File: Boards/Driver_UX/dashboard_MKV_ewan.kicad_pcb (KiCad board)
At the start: 4 copper layers, 57.2 x 41.7 mm, 63 parts, among them J1 MM_F_VT_10, J2 MM_F_VT_20, J3 MM_F_VT_04, J4 CONN_02X03, J5 CONN_02X03, Q1 SSM3K333R, U1 ATMEGA16M1, U101 TPS560430YF, U3 ATmega328P-AU, U4 CAN_Transceiver, Y1 Crystal_SMD, Y2 Crystal_SMD

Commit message: start of new layout
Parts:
- moved D101 99.3 mm to (77.9, 88.1)
- moved J3 99.1 mm to (105.4, 89.4)
- moved J1 99.1 mm to (118.0, 92.1)
- moved J2 99.1 mm to (90.1, 84.9)
- moved C102 98.9 mm to (76.6, 82.3)
- moved C103 98.9 mm to (76.5, 75.9)
- moved D102 98.9 mm to (75.9, 93.4)
- moved D103 98.9 mm to (87.2, 76.9)
- moved L101 98.9 mm to (80.2, 76.4)
- moved R104 98.9 mm to (84.1, 78.7)
- moved R105 98.9 mm to (87.2, 80.7)
- moved C101 98.9 mm to (76.4, 84.1)
- moved COUT101 98.9 mm to (77.8, 71.9)
- moved COUT102 98.9 mm to (84.1, 73.0)
- moved COUT103 98.9 mm to (80.1, 71.9)
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- renumbered PD1 to D3, PD2 to D4, PB5 to D5, PB6 to D6, PC7 to D8
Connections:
- D101 pad 1: /12V -> Net-(C101-Pad1)
- J2 pad 2: +12V -> /12V
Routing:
- net Net-(C13-Pad1): track 13.9 -> 2.25 mm, vias 2 -> 0
- net GND: track 104.2 -> 112.8 mm
- net Net-(C101-Pad1): track 16.9 -> 24.1 mm
- net /SCK: track 21.8 -> 16.7 mm, vias 3 -> 1
- net /12V: track 3.63 -> 0.00 mm
- net /STR_POT_SENSE: track 43.0 -> 39.7 mm, vias 4 -> 2
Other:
- board text removed: "Emily Wan DUX Rev 1.2 | 12/14/19 OEM-MKV"

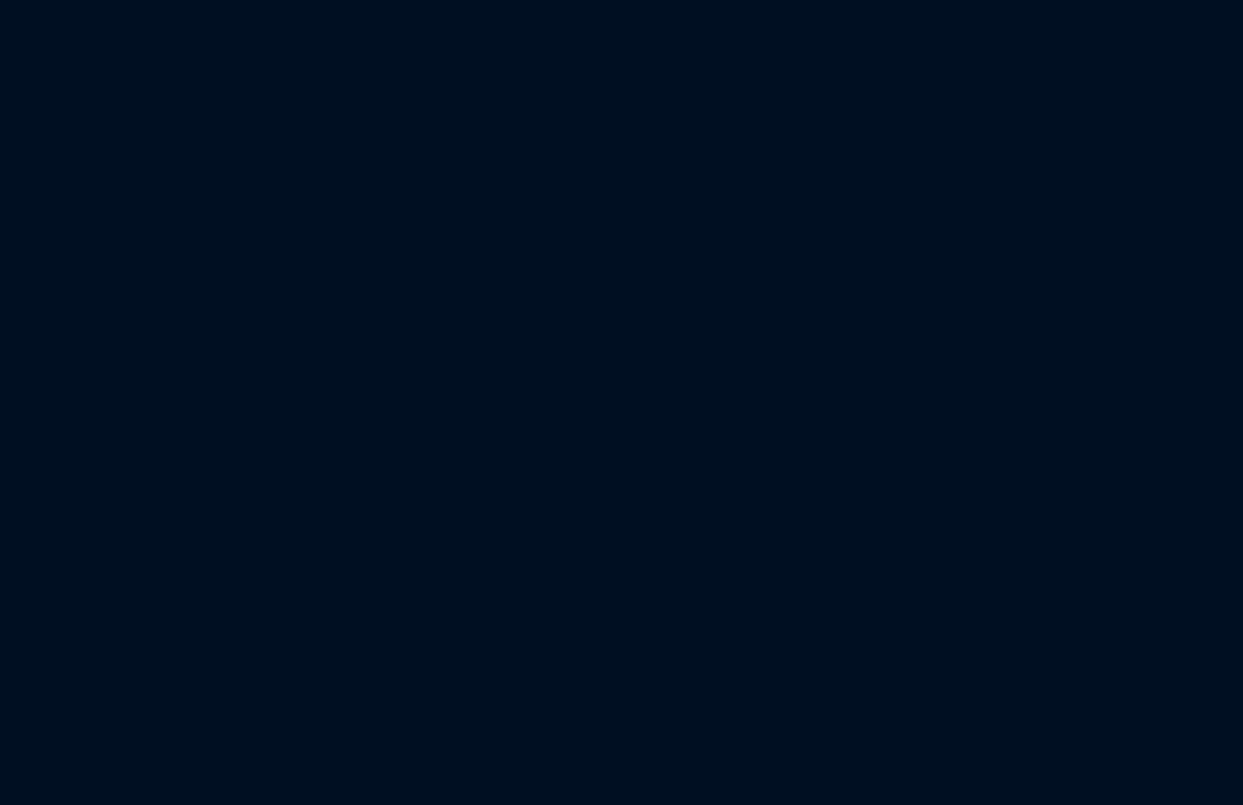
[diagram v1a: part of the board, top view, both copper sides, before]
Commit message: New Board Shape for DUX
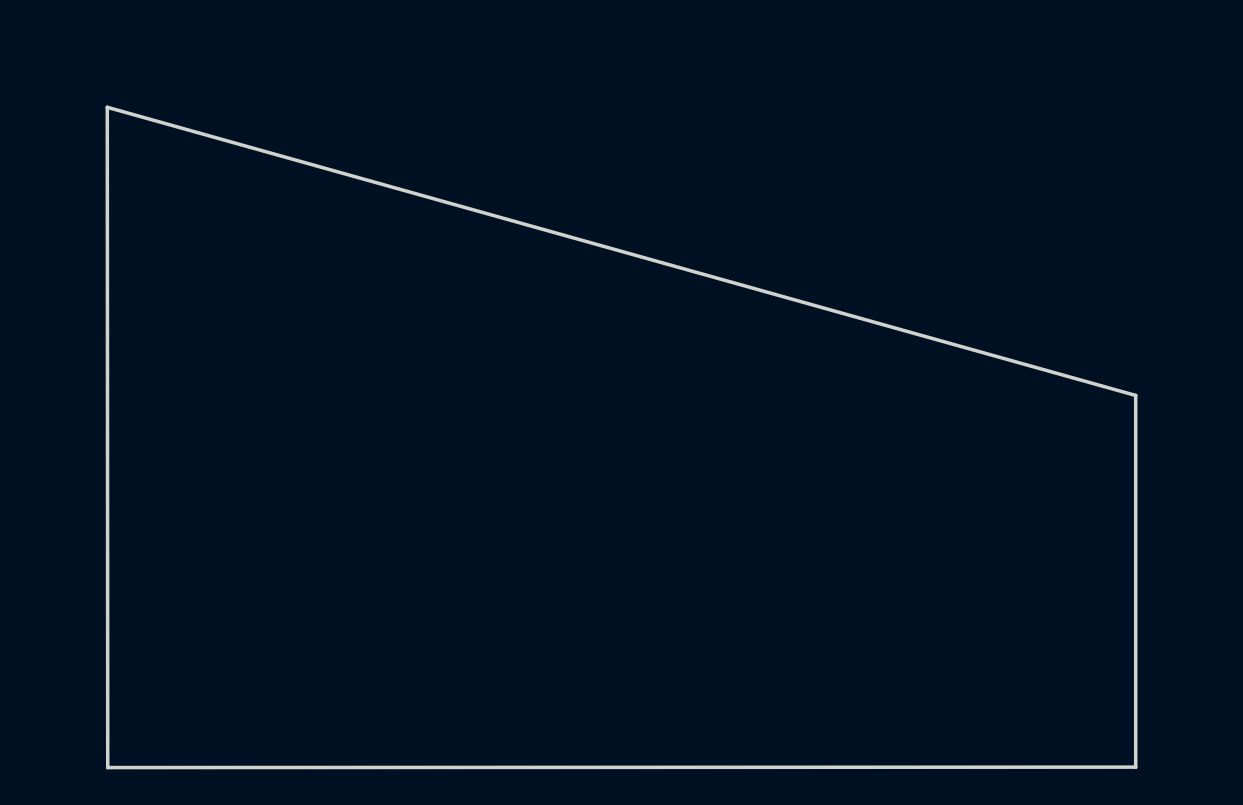
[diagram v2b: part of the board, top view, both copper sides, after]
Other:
- board size 57.2 x 41.7 mm -> 90.5 x 93 mm
- board text added: "Front"
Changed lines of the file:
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@@
-(kicad_pcb (version 20171130) (host pcbnew 5.1.4-e60b266~84~ubuntu18.04.1)
+(kicad_pcb (version 20171130) (host pcbnew "(5.1.5-0-10_14)")
   (general
     (thickness 1.6)
-    (drawings 8)
+    (drawings 35)
     (tracks 673)
     (zones 0)
@@
   )
   (setup
-    (last_trace_width 0.762)
+    (last_trace_width 0.1524)
     (user_trace_width 0.254)
     (user_trace_width 0.381)
@@
     )
   )
+  (gr_text Front (at 105.2576 145.45056) (layer F.Fab)
+    (effects (font (size 1.5 1.5) (thickness 0.3)))
+  )
+  (gr_line (start 149.43328 138.62812) (end 119.41048 138.62812) (layer F.Fab) (width 0.15))
+  (gr_line (start 152.98928 135.52932) (end 152.98928 135.55472) (layer F.Fab) (width 0.15))
+  (gr_line (start 102.08768 109.24032) (end 102.11308 146.78152) (layer Edge.Cuts) (width 0.2))
+  (gr_line (start 149.43328 143.88592) (end 149.43328 138.62812) (layer F.Fab) (width 0.15))
+  (gr_line (start 126.39548 137.35812) (end 126.39548 120.03532) (layer F.Fab) (width 0.15))
+  (gr_line (start 152.98928 145.23212) (end 158.27248 145.23212) (layer F.Fab) (width 0.15))
+  (gr_line (start 119.41048 143.91132) (end 149.43328 143.88592) (layer F.Fab) (width 0.15))
+  (gr_line (start 119.41048 138.62812) (end 119.41048 143.91132) (layer F.Fab) (width 0.15))
+  (gr_line (start 152.98928 135.55472) (end 152.98928 145.23212) (layer F.Fab) (width 0.15))
+  (gr_line (start 158.27248 135.52932) (end 152.98928 135.52932) (layer F.Fab) (width 0.15))
+  (gr_line (start 126.39548 120.03532) (end 121.11228 120.03532) (layer F.Fab) (width 0.15))
+  (gr_line (start 121.11228 120.03532) (end 121.11228 137.35812) (layer F.Fab) (width 0.15))
+  (gr_line (start 126.39548 120.03532) (end 121.11228 137.35812) (layer F.Fab) (width 0.15))
+  (gr_line (start 158.27248 145.23212) (end 158.27248 135.52932) (layer F.Fab) (width 0.15))
+  (gr_line (start 121.11228 137.35812) (end 126.39548 137.35812) (layer F.Fab) (width 0.15))
+  (gr_line (start 102.11308 146.78152) (end 160.55848 146.75612) (layer Edge.Cuts) (width 0.2))
+  (gr_line (start 149.43328 138.62812) (end 119.41048 143.91132) (layer F.Fab) (width 0.15))
+  (gr_line (start 119.41048 138.62812) (end 149.43328 143.88592) (layer F.Fab) (width 0.15))
+  (gr_line (start 160.55848 146.75612) (end 160.55848 125.62332) (layer Edge.Cuts) (width 0.2))
+  (gr_line (start 158.27248 135.52932) (end 152.98928 145.23212) (layer F.Fab) (width 0.15))
+  (gr_line (start 121.11228 120.03532) (end 126.39548 137.35812) (layer F.Fab) (width 0.15))
+  (gr_line (start 160.55848 125.62332) (end 102.08768 109.24032) (layer Edge.Cuts) (width 0.2))
+  (gr_line (start 152.98928 135.52932) (end 158.27248 145.23212) (layer F.Fab) (width 0.15))
+  (gr_text 1 (at 118.36908 143.42872) (layer F.Fab)
+    (effects (font (size 1 1) (thickness 0.15)))
+  )
+  (gr_text 1 (at 121.44248 119.17172) (layer F.Fab)
+    (effects (font (size 1 1) (thickness 0.15)))
+  )
+  (gr_text 1 (at 153.29408 134.61492) (layer F.Fab)
+    (effects (font (size 1 1) (thickness 0.15)))
+  )
   (gr_line (start 127.1778 95.4532) (end 70.0278 95.4532) (layer Edge.Cuts) (width 0.2))
   (gr_line (start 127.1778 95.4532) (end 127.1778 69.6214) (layer Edge.Cuts) (width 0.2))
@@
   (segment (start 77.7748 64.69634) (end 79.58836 62.88278) (width 0.254) (layer F.Cu) (net 1))
   (segment (start 77.7748 70.4187) (end 77.7748 64.69634) (width 0.254) (layer F.Cu) (net 1))
-  (segment (start 80.29894 88.96034) (end 80.2513 88.9127) (width 0.381) (layer F.Cu) (net 4))
   (segment (start 84.12988 81.8388) (end 85.22988 81.8388) (width 0.1524) (layer F.Cu) (net 3))
   (segment (start 87.0454 81.8388) (end 87.2282 81.656) (width 0.1524) (layer F.Cu) (net 3))
@@
   (segment (start 211.980945 83.963482) (end 210.240678 83.963482) (width 0.1524) (layer B.Cu) (net 3))
   (via (at 209.995144 84.209016) (size 0.6096) (drill 0.3048) (layers F.Cu B.Cu) (net 3))
+  (segment (start 80.29894 88.96034) (end 80.2513 88.9127) (width 0.381) (layer F.Cu) (net 4))
   (segment (start 77.5896 80.1394) (end 77.5896 79.1894) (width 0.381) (layer F.Cu) (net 4))
   (segment (start 77.5843 80.1447) (end 77.5896 80.1394) (width 0.254) (layer F.Cu) (net 4))

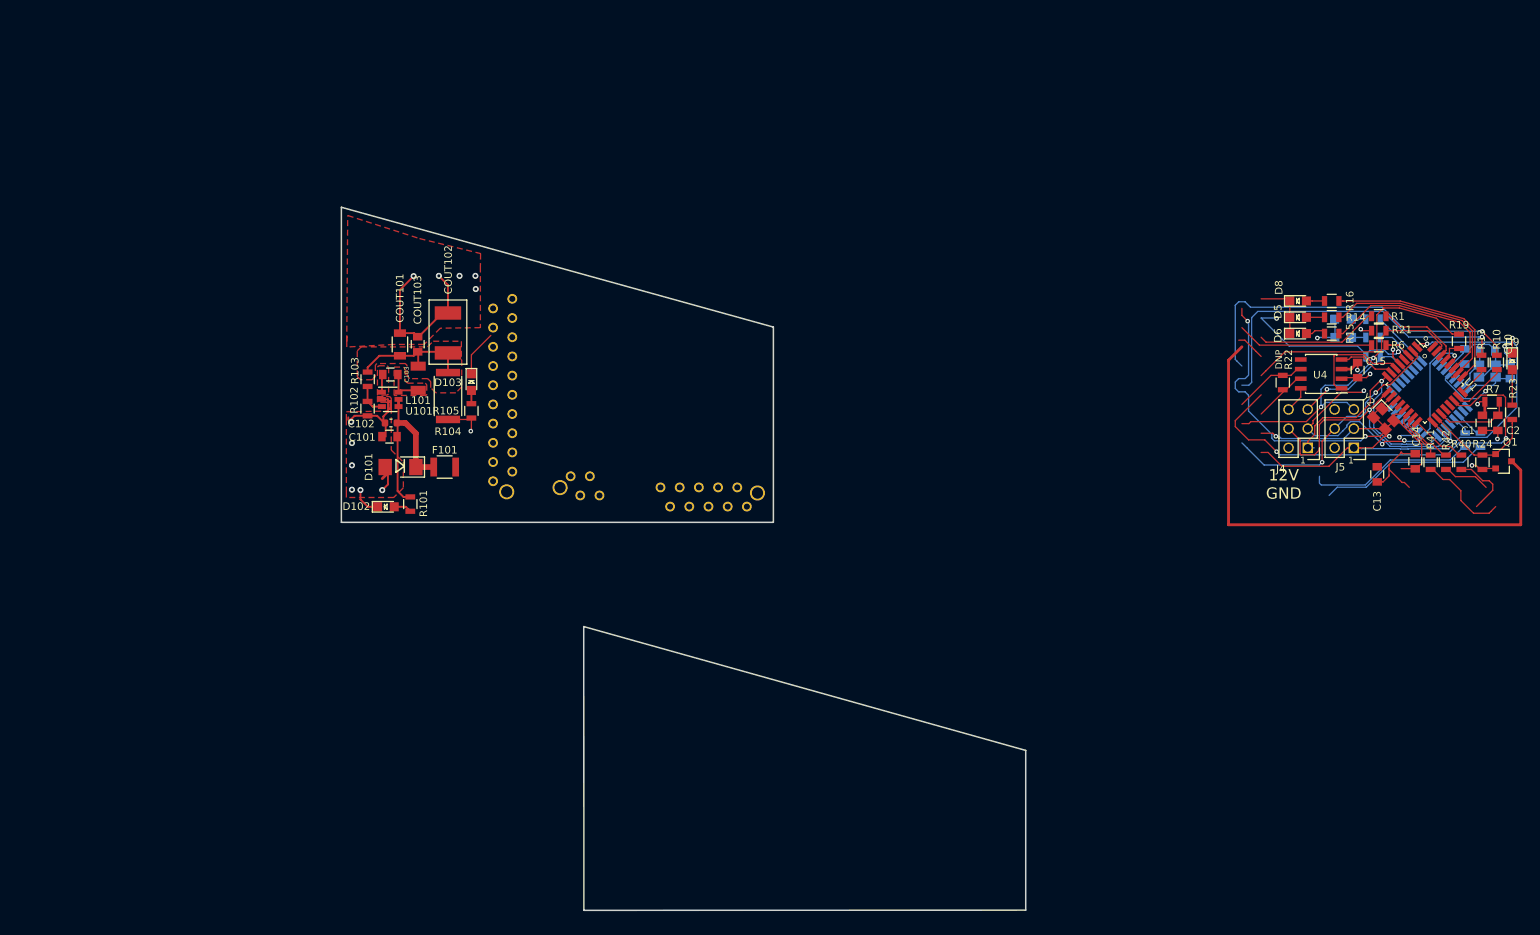
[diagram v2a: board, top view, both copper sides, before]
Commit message: 3 rev of dashboard layout
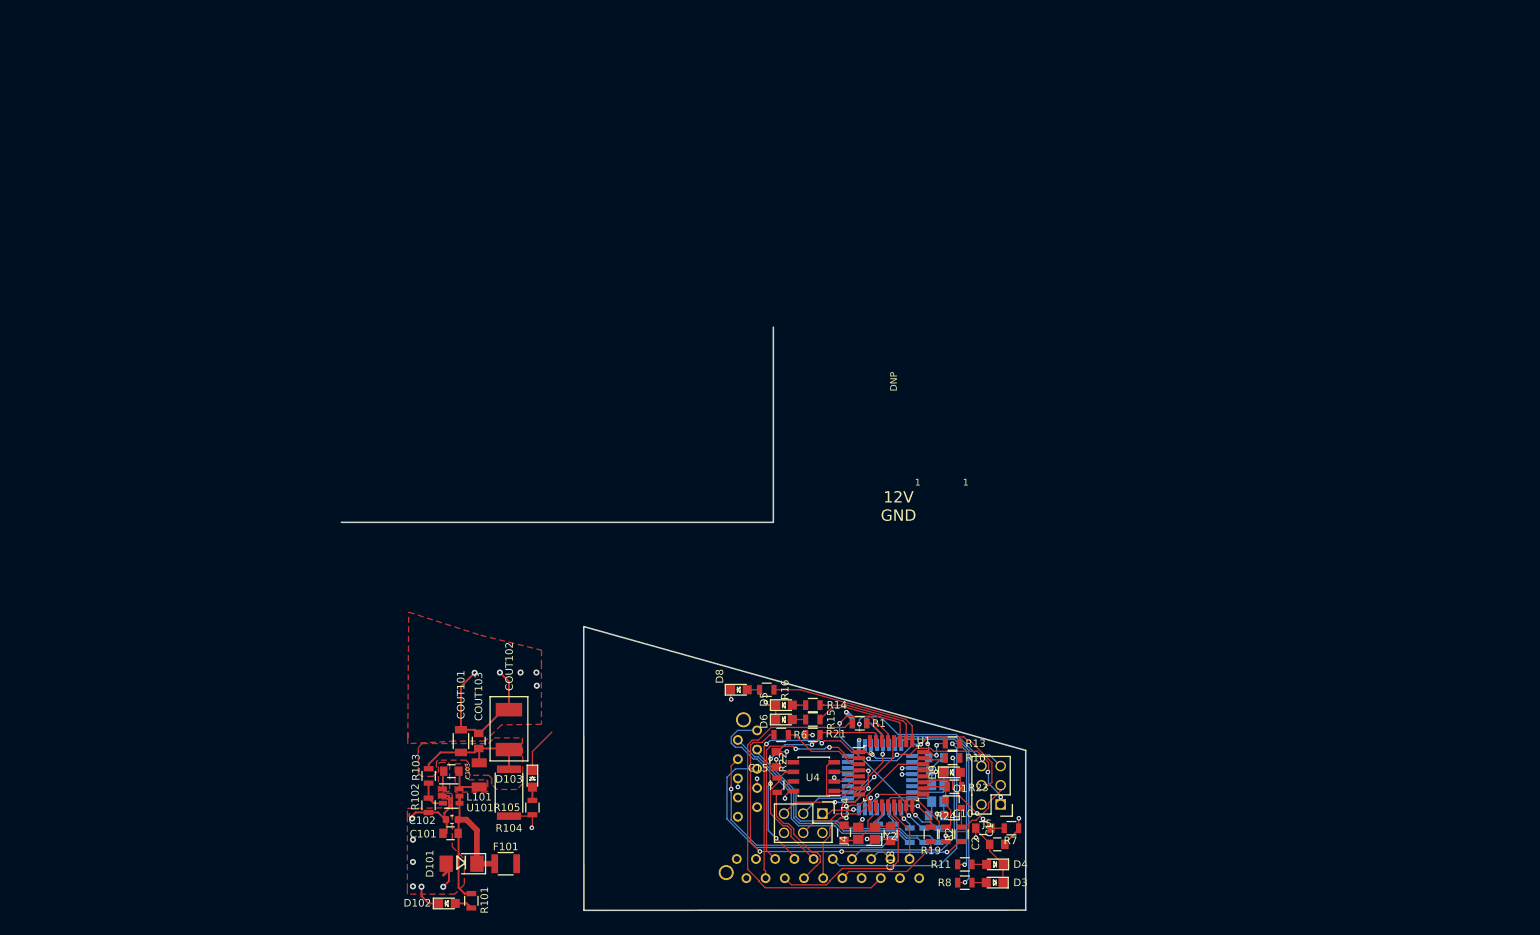
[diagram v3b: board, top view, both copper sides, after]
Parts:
- removed J3: MM_F_VT_04, footprints:micromatch_female_vert_4
- added R2: R_100, footprints:R_0805_OEM, F.Cu at (152.1, 136.7)
- D3, D4, R11, R8: moved to F.Cu
- R40, R41, R42: moved to B.Cu
- moved C10 96.0 mm to (148.7, 134.2), turned to 0 degrees
- moved R19 95.6 mm to (148.0, 136.7), turned to 270 degrees
- moved R6 94.4 mm to (128.2, 123.6)
- moved R44 93.4 mm to (143.0, 136.3)
- moved R43 93.3 mm to (141.0, 136.3)
- moved C15 92.5 mm to (127.6, 126.8), turned to 90 degrees
- moved R21 92.0 mm to (132.4, 123.6)
- moved D9 91.9 mm to (150.8, 128.5), turned to 0 degrees
- moved Y1 91.7 mm to (148.9, 131.3), turned to 270 degrees
- moved C9 91.5 mm to (148.9, 128.3), turned to 180 degrees
- moved R16 90.7 mm to (126.3, 117.6)
- moved C14 90.1 mm to (136.5, 136.5)
- moved D8 90.1 mm to (122.6, 117.6)
- moved R11 90.1 mm to (152.5, 140.7), turned to 180 degrees
- moved R8 90.1 mm to (152.5, 143.1), turned to 180 degrees
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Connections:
- J1 pad 4: GND -> /DATA_SPEED_LED_BAR
- J1 pad 5: GND -> /DATA_SOC_LED_BAR
- J1 pad 6: GND -> VCC
- Q1 pad 3: /RTD_LSD -> Net-(Q1-Pad3)
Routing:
- net /RTD_LSD: track 71.9 -> 12.9 mm, vias 0 -> 1
- net /RJLED1: track 16.3 -> 50.7 mm
- net /START_BTN: track 57.1 -> 23.9 mm
- net /STR_POT_SENSE: track 39.7 -> 7.93 mm, vias 2 -> 0
- net /SCK: track 16.7 -> 46.8 mm, vias 1 -> 0
- net /SCK_2: track 43.3 -> 17.2 mm, vias 4 -> 1
- net /HV_LED: track 6.29 -> 32.2 mm
- net Net-(R19-Pad1): track 3.15 -> 28.1 mm, vias 0 -> 2
- net /MISO_2: track 33.7 -> 8.86 mm
- net VCC: track 51.3 -> 27.6 mm
- net /MOSI_2: track 36.9 -> 13.4 mm
- net /LV_LED: track 12.1 -> 35.6 mm
- net Net-(R8-Pad2): track 6.71 -> 30.0 mm, vias 0 -> 1
- net /Brake_LED: track 8.82 -> 31.3 mm
- net /LED_IMD: track 46.8 -> 26.2 mm
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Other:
- board size 90.5 x 93 mm -> 90.5 x 77.2 mm

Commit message: finished rev4, ready for feedback
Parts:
- added G***: LOGO, footprints:Logo_Large, B.Cu at (116.9, 91.5)
- C15, R1, R19, R21, R6: moved to B.Cu
- moved R13 13.6 mm to (155.2, 137.6), turned to 0 degrees
- moved R7 11.7 mm to (150.4, 127.7)
- moved C2 11.1 mm to (150.3, 125.8), turned to 0 degrees
- moved R10 11.0 mm to (151.7, 137.6), turned to 0 degrees
- moved C1 10.8 mm to (150.2, 129.6)
- moved R1 10.3 mm to (128.3, 121.6)
- moved D9 8.90 mm to (156.2, 135.6), turned to 180 degrees
- moved R16 7.30 mm to (133.3, 119.7)
- moved PC7 7.14 mm to (129.4, 119.7)
- moved R19 6.20 mm to (154.2, 137.2)
- moved R23 5.35 mm to (152.5, 135.6)
- moved C15 5.05 mm to (132.4, 128.2), turned to 270 degrees
- moved R2 4.17 mm to (148.0, 137.5), turned to 180 degrees
- moved U101 3.84 mm to (88.4, 132.0)
- moved C102 3.84 mm to (88.5, 135.1)
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- renumbered D5 to PB5, D6 to PB6, D8 to PC7, D3 to PD1, D4 to PD2
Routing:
- net GND: track 92.9 -> 119.9 mm, vias 24 -> 20
- net Net-(R13-Pad2): track 4.52 -> 22.3 mm, vias 2 -> 0
- net Net-(R10-Pad2): track 3.13 -> 19.6 mm
- net /LED_START: track 32.8 -> 21.6 mm
- net /RJLED1: track 50.7 -> 39.6 mm, vias 0 -> 2
- net /LED_IMD: track 26.2 -> 15.5 mm
- net Net-(R1-Pad2): track 3.52 -> 14.1 mm, vias 0 -> 1
- net VCC: track 27.6 -> 37.4 mm, vias 9 -> 8
- net Net-(C2-Pad1): track 14.3 -> 5.95 mm, vias 2 -> 0
- net Net-(R16-Pad1): track 21.2 -> 13.9 mm
- net /LED_BMS: track 14.2 -> 21.0 mm, vias 0 -> 1
- net /STR_POT_SENSE: track 7.93 -> 13.9 mm, vias 0 -> 1
- net Net-(R19-Pad1): track 28.1 -> 24.4 mm, vias 2 -> 1
- net /SCK: track 46.8 -> 50.5 mm
- net Net-(Q1-Pad3): track 2.56 -> 5.81 mm
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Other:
- board text added: "Emily Wan Driver UX REV 4 4/24/2020 OEM-MKV"

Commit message: Rev 5 Ready for feedback :)
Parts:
- removed G***: LOGO, footprints:Logo_Large
- added TP1: TP_12V, footprints:tp_1.6mm, F.Cu at (117.6, 145.0)
- added TP2: TP_CANL, footprints:tp_1.6mm, F.Cu at (125.4, 117.6)
- added TP3: TP_5V, footprints:tp_1.6mm, F.Cu at (152.1, 145.0)
- added TP4: TP_CANH, footprints:tp_1.6mm, F.Cu at (121.8, 117.6)
- added TP5: TP_GND, footprints:tp_1.6mm, F.Cu at (157.2, 145.0)
- moved D3 0.96 mm to (156.9, 142.5)
- moved R8 0.96 mm to (153.0, 142.5)
- moved D4 0.59 mm to (156.9, 140.5)
- moved R11 0.59 mm to (153.0, 140.5)
- moved C1 0.12 mm to (150.3, 129.6), turned to 0 degrees
- renumbered PD1 to D3, PD2 to D4, PB5 to D5, PB6 to D6, PC7 to D8
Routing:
- net /CANH: track 19.4 -> 40.2 mm, vias 0 -> 1
- net /CANL: track 18.1 -> 30.1 mm, vias 0 -> 1
- net VCC: track 37.4 -> 44.9 mm, vias 8 -> 7
- net /12V: track 0.00 -> 7.04 mm
- net /LED_BMS: track 21.0 -> 25.3 mm
- net Net-(R11-Pad2): track 24.4 -> 26.8 mm
- net Net-(R8-Pad2): track 29.2 -> 31.2 mm
- net GND: track 119.9 -> 118.8 mm, vias 20 -> 19
- net /RJLED2: track 38.6 -> 39.3 mm
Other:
- board size 90.5 x 77.2 mm -> 58.5 x 37.5 mm
- board text added: "PB5"
- board text added: "PB6"
- board text added: "PC7"
- board text added: "PD1"
- board text added: "PD2"
- board text removed: "12V GND"
